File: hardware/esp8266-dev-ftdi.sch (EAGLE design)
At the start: 32 parts, among them CON1 USBMICRO-NO_CENTER

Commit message: schematic mostly done
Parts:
- removed ESP-UART: (no value), p.peter-connectors:GENERIC-1X6STANDARD
- removed L2, L3, L4, L5, L6: WS2812S, p.peter-leds:WS2812S
- removed RX, TX: (no value), p.peter-leds:LED0603
- added F1: 500mA, p.peter-regulators:FUSE0805
- added LED-RX, LED-TX: (no value), p.peter-leds:LED0805
- added LED2, LED3, LED4, LED5, LED6: (no value), p.peter-leds:WS2812B
- added R10, R9: 2k, p.peter-rcl:R-EU_R0603
- added SJ1: (no value), jumper:SJ
- added SJ2: (no value), jumper:SJ2W
- added SW2, SW3, SW4: (no value), p.peter-passives:SWITCH-DEFAULT_OFF-2PIN
- L1: value (none) -> 875-MI0805K601R-10; device dp_devices:FERRITE-0603 -> p.peter-passives:INDUCTOR0805
- LED1: device p.peter-leds:LED0603 -> p.peter-leds:LED0805
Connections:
- new net N$12: LED2.DO, LED3.DI
- new net N$15: LED3.DO, LED4.DI
- new net N$16: LED4.DO, LED5.DI
- new net N$17: LED5.DO, LED6.DI
- new net N$18: CON1.VBUS, F1.P$2, SJ1.2
- new net N$20: R9.2, SW3.P$1
- new net N$21: R10.2, SW4.P$1
- new net VCCIO: SJ2.2, U$1.VCCIO, U$2.VCC
- net +3V3: now also SJ2.3; no longer ESP-UART.3, U$1.VCCIO
- net +5V: now also LED2.VCC, LED3.VCC, LED4.VCC, LED5.VCC, LED6.VCC, SJ2.1; no longer U$2.VCC
- net /SLEEP: now also U$2.DTR
- net CTS: now also U$2.CTS
- net GND: now also LED-RX.C, LED-TX.C, LED2.GND, LED3.GND, LED4.GND, LED5.GND, LED6.GND, R10.1, R9.1, SW2.P$1; no longer ESP-UART.1, RX.C, TX.C
- net IO2: now also LED2.DI
- net N$10: now also SW2.P$2
- net N$2: now also F1.P$1, SJ1.1; no longer CON1.VBUS
- net N$3: now also LED-TX.A; no longer TX.A
- net N$8: now also LED-RX.A; no longer RX.A
- net RX: now also SW4.P$2; no longer ESP-UART.5
- net TX: now also SW3.P$2; no longer ESP-UART.4
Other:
- note added: "TODO: - Footprints for 2mm V12, Breakoutboard - Prototype area with - lengthen USB contacts - Hooks for rubber band - Hole for lanyard"
- note removed: "TODO: - Fuse - Footprints for 2mm V12, Breakoutboard - Prototype area with -- LEDs -- BUTTON -- Thermristor - Correct LEDs - Battery contacts - lengthen USB contacts - Hooks for rubber band - Hole for lanyard"
- moved on the sheet: C2, Q1, R6, R7, R8, RF1, SW1

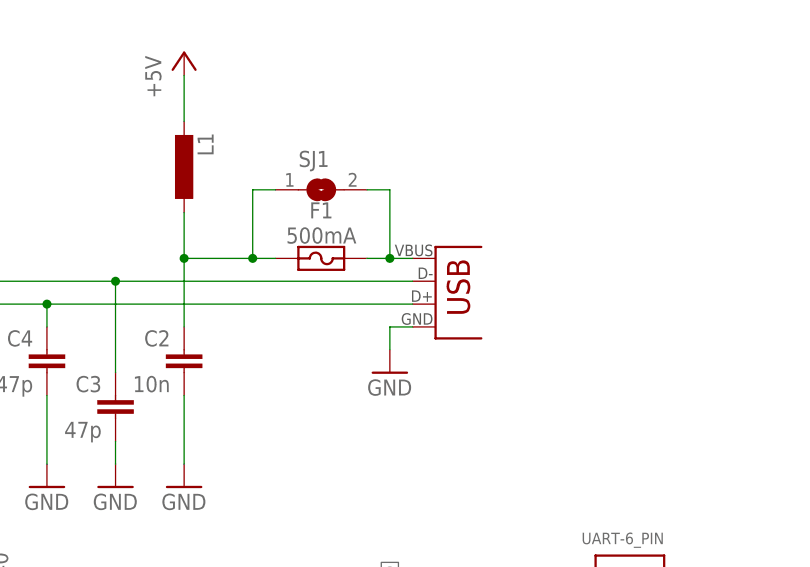
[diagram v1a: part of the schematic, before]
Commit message: new USB connector with longer pads
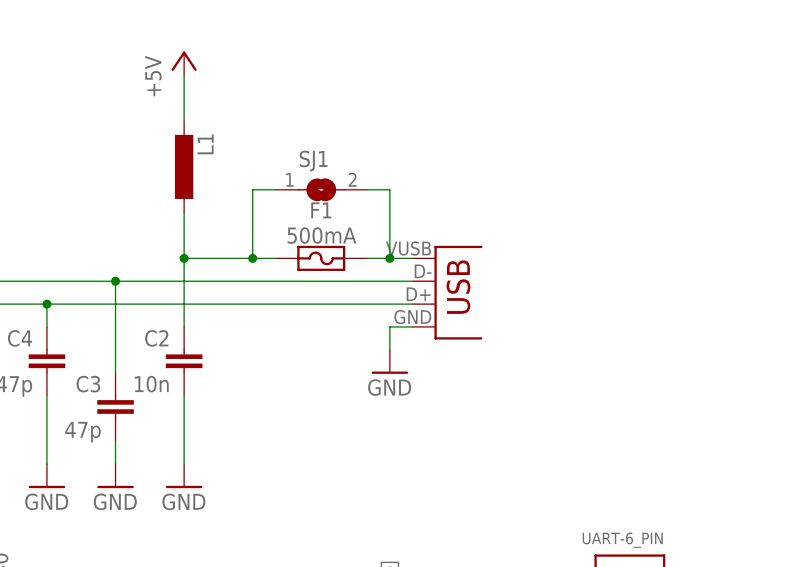
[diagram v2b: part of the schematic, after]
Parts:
- CON1: value USBMICRO-NO_CENTER -> USBMICRO-NO_CENTER-LONG_PADS; device p.peter-connectors:USBMICRO-NO_CENTER -> p.peter-connectors:USBMICRO-NO_CENTER-LONG_PADS
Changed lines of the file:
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@@
 <part name="GND1" library="supply1" deviceset="GND" device=""/>
 <part name="L1" library="p.peter-passives" deviceset="INDUCTOR" device="0805" value=" 875-MI0805K601R-10"/>
-<part name="CON1" library="p.peter-connectors" deviceset="USB" device="MICRO-NO_CENTER"/>
+<part name="CON1" library="p.peter-connectors" deviceset="USB" device="MICRO-NO_CENTER-LONG_PADS" value="USBMICRO-NO_CENTER-LONG_PADS"/>
 <part name="P+2" library="supply1" deviceset="+5V" device=""/>
 <part name="R1" library="p.peter-rcl" deviceset="R-EU_" device="R0603" value="27"/>
